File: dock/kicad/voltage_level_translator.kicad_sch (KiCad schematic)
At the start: 21 parts, among them Q1 2SK2009, SW1 TA-3532S-A2, U3 TS5A3157DBVR, U4 TXS0108EPW, U5 TXS0108EPW, U6 TMUX1574PW, U7 TMUX1574PW

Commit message: Added testpoints, J3 mirrored
- J3 mirrored in order to share the same pin numbers with CN1. It just makes it less confusing.

- Added test points on power supplies, and SEL signals just to help test the board.
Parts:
- added TP5: VTARGET, TestPoint:TestPoint_Pad_D1.0mm, symbol Connector:TestPoint
- added TP6: SEL, TestPoint:TestPoint_Pad_D1.0mm, symbol Connector:TestPoint
- added TP7: ~{SEL}, TestPoint:TestPoint_Pad_D1.0mm, symbol Connector:TestPoint
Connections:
- net SEL: now also TP6.1
- net VTARGET: now also TP5.1
- net ~{SEL}: now also TP7.1

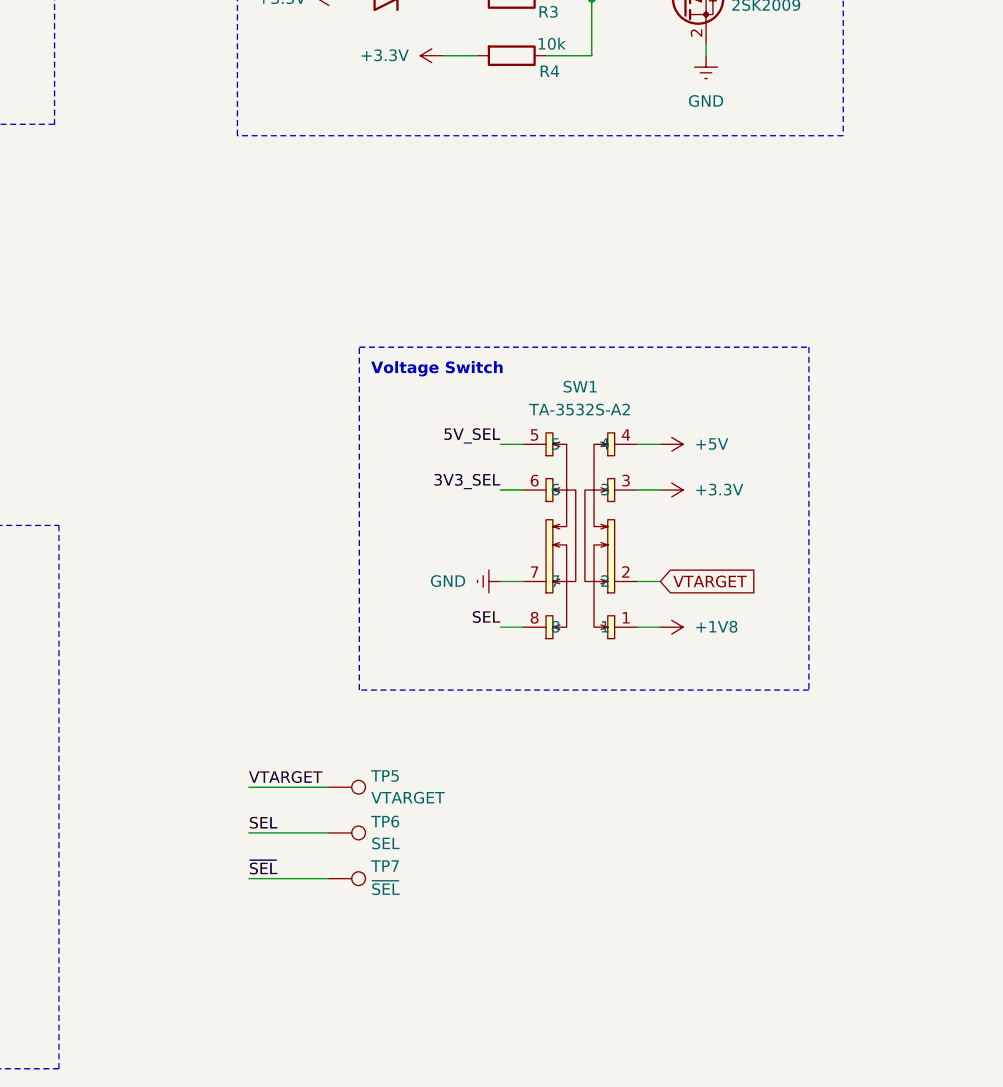
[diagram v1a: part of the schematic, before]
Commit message: Modified test pads & added TC2050
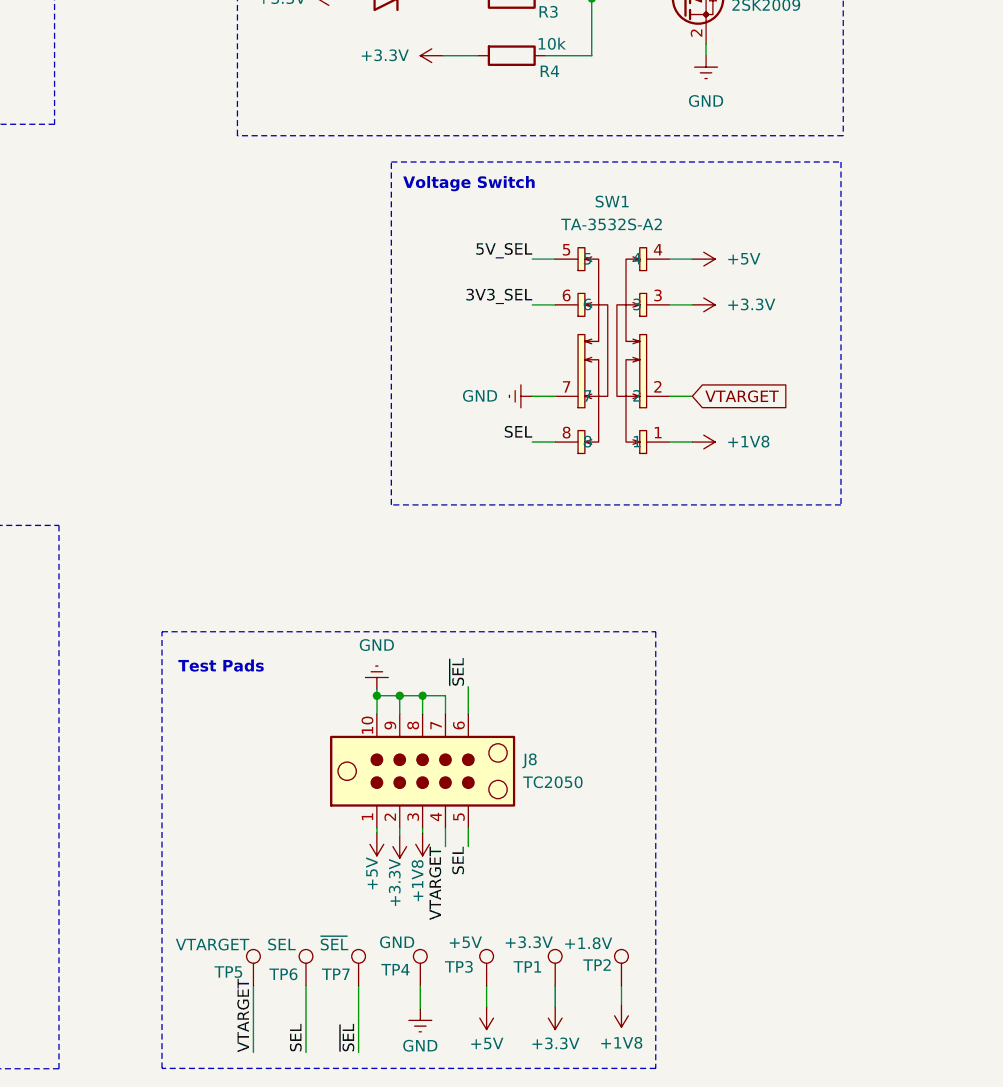
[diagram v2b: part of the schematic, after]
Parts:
- added J8: TC2050, Connector:Tag-Connect_TC2050-IDC-NL_2x05_P1.27mm_Vertical_with_bottom_clip, symbol Connector:TC2050
- added TP1: +3.3V, TestPoint:TestPoint_Pad_D1.0mm, symbol Connector:TestPoint
- added TP2: +1.8V, TestPoint:TestPoint_Pad_D1.0mm, symbol Connector:TestPoint
- added TP3: +5V, TestPoint:TestPoint_Pad_D1.0mm, symbol Connector:TestPoint
- added TP4: GND, TestPoint:TestPoint_Pad_D1.0mm, symbol Connector:TestPoint
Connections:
- net +1V8: now also J8.3, TP2.1
- net +3.3V: now also J8.2, TP1.1
- net +5V: now also J8.1, TP3.1
- net GND: now also J8.10, J8.7, J8.8, J8.9, TP4.1
- net SEL: now also J8.5
- net VTARGET: now also J8.4
- net ~{SEL}: now also J8.6
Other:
- note added: "Test Pads"
- moved on the sheet: SW1, TP5, TP6, TP7

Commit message: Changed VTarget to Vio
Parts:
- TP5: value VTARGET -> VIO
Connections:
- net VTARGET renamed VIO
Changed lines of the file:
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@@
 		)
 	)
-	(label "VTARGET"
+	(label "VIO"
 		(at 138.684 162.814 270)
 		(effects
@@
 		)
 	)
-	(label "VTARGET"
+	(label "VIO"
 		(at 117.348 185.674 90)
 		(effects
@@
 		)
 	)
-	(global_label "VTARGET"
+	(global_label "VIO"
 		(shape input)
 		(at 36.83 69.85 0)
@@
 		)
 		(property "Intersheetrefs" "${INTERSHEET_REFS}"
-			(at 47.6166 69.85 0)
+			(at 42.8391 69.85 0)
 			(effects
 				(font
@@
 		)
 	)
-	(global_label "VTARGET"
+	(global_label "VIO"
 		(shape input)
 		(at 40.64 107.95 180)
@@
 		)
 		(property "Intersheetrefs" "${INTERSHEET_REFS}"
-			(at 29.8534 107.95 0)
+			(at 34.6309 107.95 0)
 			(effects
 				(font
@@
 		)
 	)
-	(global_label "VTARGET"
+	(global_label "VIO"
 		(shape input)
 		(at 166.116 112.776 0)
@@
 		)
 		(property "Intersheetrefs" "${INTERSHEET_REFS}"
-			(at 176.9026 112.776 0)
+			(at 172.1251 112.776 0)
 			(effects
 				(font
@@
 			)
 		)
-		(property "Value" "VTARGET"
-			(at 108.712 173.736 0)
+		(property "Value" "VIO"
+			(at 113.03 173.736 0)
 			(effects
 				(font

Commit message: Minor schematic changes
- Added net classes
- Added cosmetic changes
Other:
- note added: "Debug Interface"
- note removed: "Test Pads"
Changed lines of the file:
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@@
 	(rectangle
 		(start 217.17 19.05)
-		(end 278.13 158.75)
+		(end 282.956 158.75)
 		(stroke
 			(width 0)
@@
 		)
 	)
-	(text "Test Pads"
+	(text "Debug Interface"
 		(exclude_from_sim no)
-		(at 113.792 143.002 0)
+		(at 116.586 141.732 0)
 		(effects
 			(font
@@
 		)
 	)
+	(rule_area
+		(polyline
+			(pts
+				(xy 262.89 37.592) (xy 275.844 37.592) (xy 275.844 60.706) (xy 275.844 67.818) (xy 263.144 67.818)
+			)
+			(stroke
+				(width 0)
+				(type dash)
+			)
+			(fill
+				(type none)
+			)
+		)
+	)
+	(rule_area
+		(polyline
+			(pts
+				(xy 262.89 107.188) (xy 275.844 107.188) (xy 275.844 130.302) (xy 275.844 137.414) (xy 263.144 137.414)
+			)
+			(stroke
+				(width 0)
+				(type dash)
+			)
+			(fill
+				(type none)
+			)
+		)
+	)
+	(rule_area
+		(polyline
+			(pts
+				(xy 69.215 144.78) (xy 93.345 144.78) (xy 93.472 172.974) (xy 93.218 173.228) (xy 69.596 173.228)
+				(xy 69.342 172.974)
+			)
+			(stroke
+				(width 0)
+				(type dash)
+			)
+			(fill
+				(type none)
+			)
+		)
+	)
+	(netclass_flag ""
+		(length 2.54)
+		(shape round)
+		(at 262.89 107.188 0)
+		(fields_autoplaced yes)
+		(effects
+			(font
+				(size 1.27 1.27)
+			)
+			(justify left bottom)
+		)
+		(property "Netclass" "LEVEL_TRANSLATION"
+			(at 263.5885 104.648 0)
+			(effects
+				(font
+					(size 1.27 1.27)
+				)
+				(justify left)
+			)
+		)
+		(property "Component Class" ""
+			(at 136.398 -44.958 0)
+			(effects
+				(font
+					(size 1.27 1.27)
+					(italic yes)
+				)
+			)
+		)
+	)
+	(netclass_flag ""
+		(length 2.54)
+		(shape round)
+		(at 164.846 112.776 0)
+		(effects
+			(font
+				(size 1.27 1.27)
+			)
+			(justify left bottom)
+		)
+		(property "Netclass" "PWR"
+			(at 163.068 108.712 0)
+			(effects
+				(font
+					(size 1.27 1.27)
+				)
+				(justify left)
+			)
+		)
+		(property "Component Class" ""
+			(at 145.288 445.77 90)
+			(effects
+				(font
+					(size 1.27 1.27)
+					(italic yes)
+				)
+			)
+		)
+	)
+	(netclass_flag ""
+		(length 2.54)
+		(shape round)
+		(at 69.342 144.78 0)
+		(fields_autoplaced yes)
+		(effects
+			(font
+				(size 1.27 1.27)
+			)
+			(justify left bottom)
+		)
+		(property "Netclass" "LEVEL_TRANSLATION"
+			(at 70.0405 142.24 0)
+			(effects
+				(font
+					(size 1.27 1.27)
+				)
+				(justify left)
+			)
+		)
+		(property "Component Class" ""
+			(at -57.15 -7.366 0)
+			(effects
+				(font
+					(size 1.27 1.27)
+					(italic yes)
+				)
+			)
+		)
+	)
+	(netclass_flag ""
+		(length 2.54)
+		(shape round)
+		(at 262.89 37.592 0)
+		(fields_autoplaced yes)
+		(effects
+			(font
+				(size 1.27 1.27)
+			)
+			(justify left bottom)
+		)
+		(property "Netclass" "LEVEL_TRANSLATION"
+			(at 263.5885 35.052 0)
+			(effects
+				(font
+					(size 1.27 1.27)
+				)
+				(justify left)
+			)
+		)
+		(property "Component Class" ""
+			(at 136.398 -114.554 0)
+			(effects
+				(font
+					(size 1.27 1.27)
+					(italic yes)
+				)
+			)
+		)
+	)
 	(symbol
 		(lib_id "power:+1V8")
@@
 		)
 		(instances
-			(project ""
+			(project "ESP32-Bus-Pirate-Dock"
 				(path "/07b4bde2-66d8-4845-8f7d-da280a4d29f6/4e83f8d5-a547-42b8-8426-b71a9f8b331b"
 					(reference "SW1")
@@
 		)
 		(instances
-			(project ""
+			(project "ESP32-Bus-Pirate-Dock"
 				(path "/07b4bde2-66d8-4845-8f7d-da280a4d29f6/4e83f8d5-a547-42b8-8426-b71a9f8b331b"
 					(reference "J8")
@@
 		)
 		(instances
-			(project ""
+			(project "ESP32-Bus-Pirate-Dock"
 				(path "/07b4bde2-66d8-4845-8f7d-da280a4d29f6/4e83f8d5-a547-42b8-8426-b71a9f8b331b"
 					(reference "U5")
@@
 		)
 		(instances
-			(project ""
+			(project "ESP32-Bus-Pirate-Dock"
 				(path "/07b4bde2-66d8-4845-8f7d-da280a4d29f6/4e83f8d5-a547-42b8-8426-b71a9f8b331b"
 					(reference "U3")
@@
 		)
 		(instances
-			(project ""
+			(project "ESP32-Bus-Pirate-Dock"
 				(path "/07b4bde2-66d8-4845-8f7d-da280a4d29f6/4e83f8d5-a547-42b8-8426-b71a9f8b331b"
 					(reference "U6")
@@
 		)
 		(instances
-			(project ""
+			(project "ESP32-Bus-Pirate-Dock"
 				(path "/07b4bde2-66d8-4845-8f7d-da280a4d29f6/4e83f8d5-a547-42b8-8426-b71a9f8b331b"
 					(reference "TP5")
